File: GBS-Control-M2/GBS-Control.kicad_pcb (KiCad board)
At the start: 2 copper layers, 38.7 x 27.3 mm, 16 parts, among them J1 PROG, U1 PLCC-44 socket, U2 ESP-M2

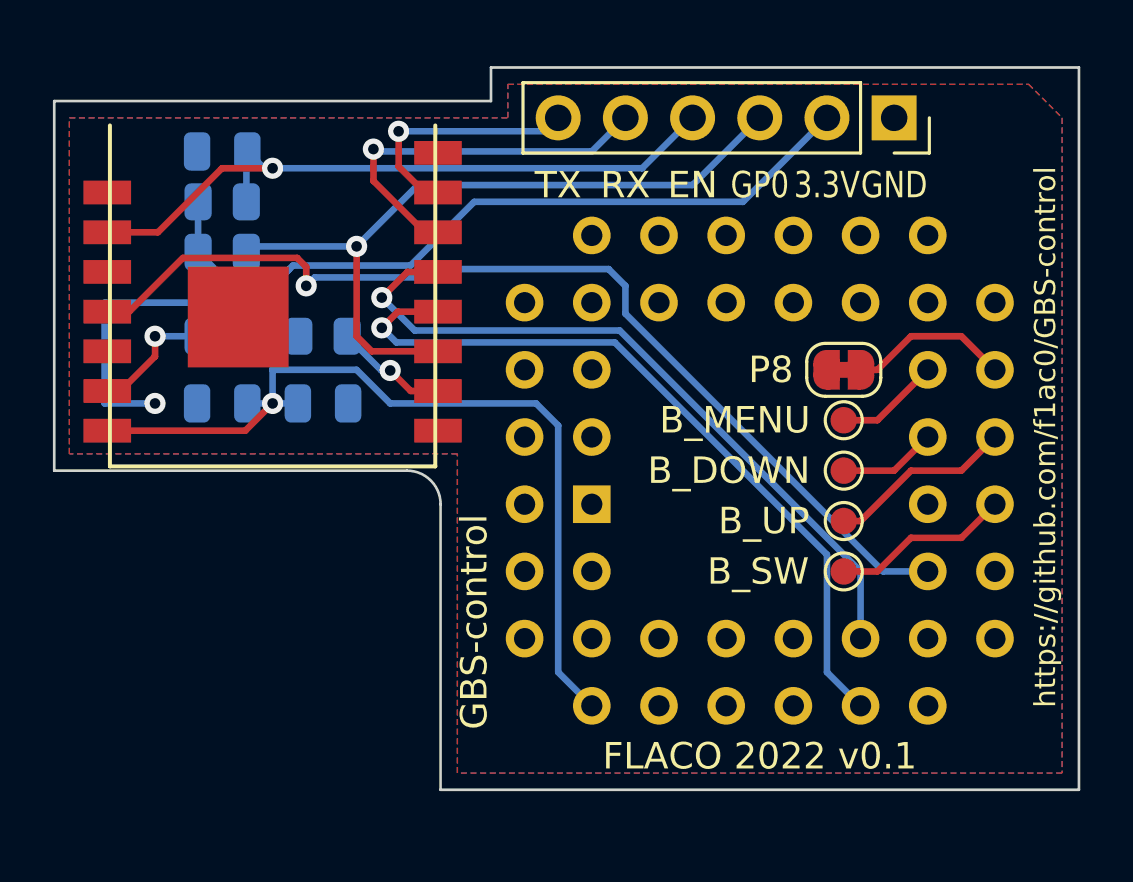
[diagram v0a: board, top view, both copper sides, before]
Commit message: KiCAD : add a port to connect the Si5351 Clock Generator
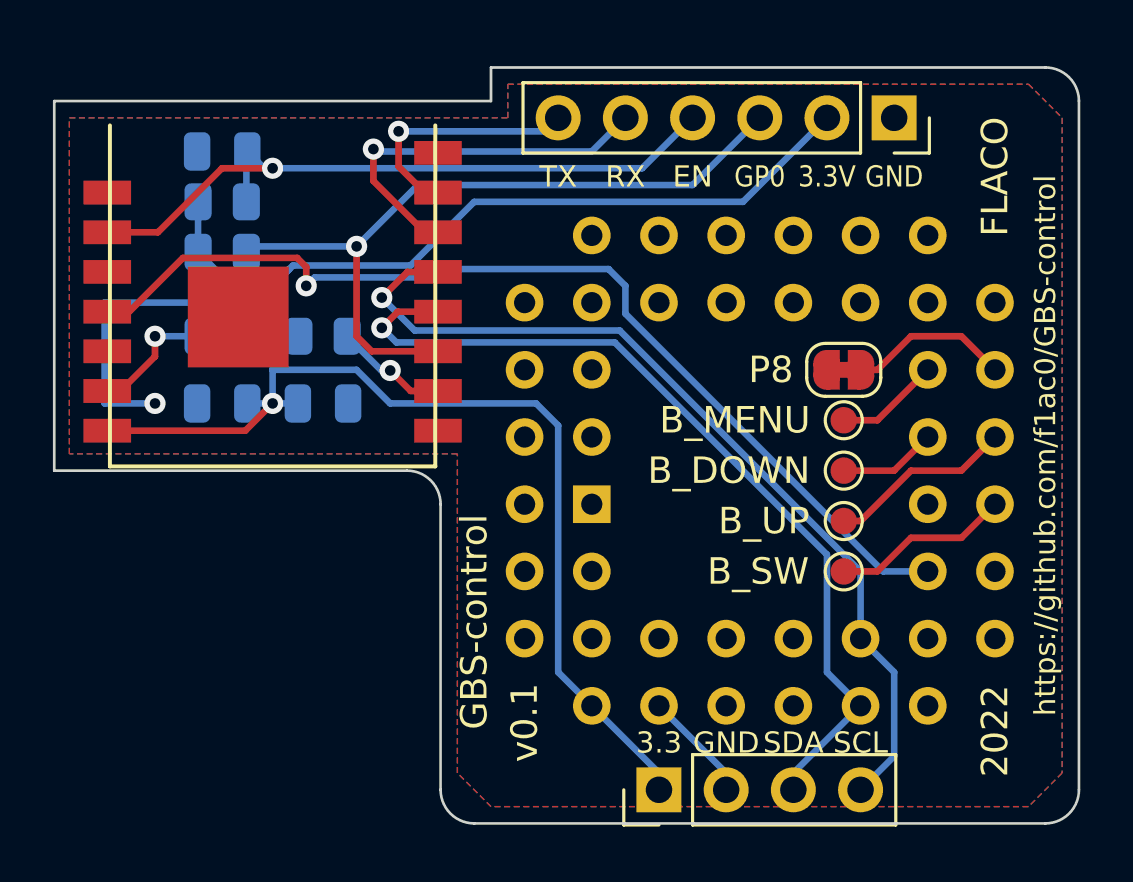
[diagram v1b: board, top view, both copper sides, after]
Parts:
- added J2: Clock port, Connector_PinHeader_2.54mm:PinHeader_1x04_P2.54mm_Vertical, F.Cu at (138.4, 102.9)
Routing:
- net /SCL: track 27.4 -> 34.2 mm
- net /SDA: track 29.0 -> 33.2 mm
- net +3.3V: track 66.5 -> 70.8 mm
- net GND: track 11.8 -> 16.0 mm
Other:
- board size 38.7 x 27.3 mm -> 38.7 x 28.6 mm
- board text added: "2022"
- board text added: "3.3"
- board text added: "FLACO"
- board text added: "SCL"
- board text added: "SDA"
- board text added: "v0.1"

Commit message: GBS-Control-12F, GBS-Control-M2 : update socket symbol and footprint, no PCB change
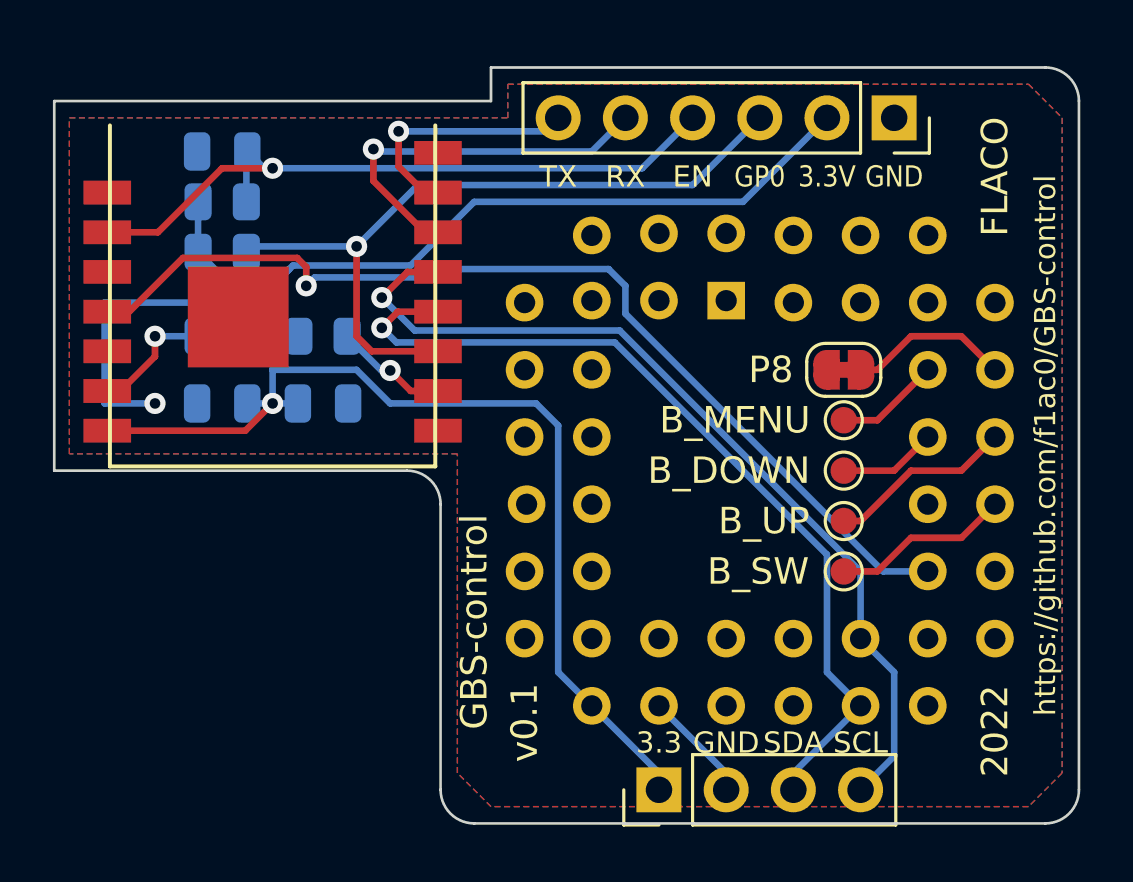
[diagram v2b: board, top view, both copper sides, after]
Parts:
- U1: footprint Package_LCC:PLCC-44_THT-Socket -> Sassa:PLCC-44_THT-SocketOnTop
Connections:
- U1 pad 18: unconnected-(U1-Pad18) -> +3.3V
- U1 pad 20: /DISABLE -> GND
- U1 pad 21: /B_MENU -> unconnected-(U1-Pad21)
- U1 pad 22: /B_UP -> unconnected-(U1-Pad22)
- U1 pad 23: /B_DOWN -> unconnected-(U1-Pad23)
- U1 pad 24: /B_SW -> unconnected-(U1-Pad24)
- U1 pad 25: unconnected-(U1-Pad25) -> /SCL
- U1 pad 26: /RESET -> /SDA
- U1 pad 27: /DEBUG -> unconnected-(U1-Pad27)
- U1 pad 30: unconnected-(U1-Pad30) -> /DEBUG
- U1 pad 31: /SDA -> /RESET
- U1 pad 32: /SCL -> unconnected-(U1-Pad32)
- U1 pad 33: unconnected-(U1-Pad33) -> /B_SW
- U1 pad 34: unconnected-(U1-Pad34) -> /B_DOWN
- U1 pad 35: unconnected-(U1-Pad35) -> /B_UP
- U1 pad 36: unconnected-(U1-Pad36) -> /B_MENU
- U1 pad 37: GND -> /DISABLE
- U1 pad 39: +3.3V -> unconnected-(U1-Pad39)
